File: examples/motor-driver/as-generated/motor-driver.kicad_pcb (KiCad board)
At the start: 2 copper layers, 88 x 50 mm, 12 parts, among them J1 VM 2.7-10.8V, J2 MOTOR A, J3 MOTOR B, J4 LOGIC, U1 DRV8833PW

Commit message: Arc out of a reversal at the line-out, and put the pour wedges back
Two corrections from review. The reversal now turns through every
intermediate 45 right where the line leaves the part - nine o'clock,
half-past ten, twelve, half-past one, three - by retracting along the
incoming leg and solving the arc onto the outgoing straight; the fold's
corners disappear instead of being spread, and the old three-millimetre
ride to the fan column goes with them. And the round-thirteen tongue
pruning is reverted: it was built on a misreading of the circles - the
pour filling a bent corner was never the complaint - so the fill goes
back to what the sweep makes of the copper.

Co-Authored-By: Claude Fable 5 <noreply@anthropic.com>
Claude-Session: https://claude.ai/code/session_01DUj7Ltu92tWg159mCSacwY
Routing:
- net /nFAULT: track 68.6 -> 65.3 mm
- net /nSLEEP: track 62.9 -> 59.6 mm
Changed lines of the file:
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@@
 	(segment (start 141.1375 83.725) (end 137.5 83.725) (width 0.25) (layer "F.Cu") (net 15))
 	(segment (start 137.5 83.725) (end 134.875 81.1) (width 0.25) (layer "F.Cu") (net 15))
-	(segment (start 134.875 81.1) (end 132.6 81.1) (width 0.25) (layer "F.Cu") (net 15))
-	(segment (start 132.6 81.1) (end 132.0 80.5) (width 0.25) (layer "F.Cu") (net 15))
-	(segment (start 132.0 80.5) (end 132.0 79.9) (width 0.25) (layer "F.Cu") (net 15))
-	(segment (start 132.0 79.9) (end 133.4 78.5) (width 0.25) (layer "F.Cu") (net 15))
-	(segment (start 133.4 78.5) (end 134.5 78.5) (width 0.25) (layer "F.Cu") (net 15))
+	(segment (start 134.875 81.1) (end 134.575 81.1) (width 0.25) (layer "F.Cu") (net 15))
+	(segment (start 134.575 81.1) (end 133.7915 80.3165) (width 0.25) (layer "F.Cu") (net 15))
+	(segment (start 133.7915 80.3165) (end 133.7915 79.2085) (width 0.25) (layer "F.Cu") (net 15))
+	(segment (start 133.7915 79.2085) (end 134.5 78.5) (width 0.25) (layer "F.Cu") (net 15))
 	(segment (start 134.5 78.5) (end 173.75 78.5) (width 0.25) (layer "F.Cu") (net 15))
 	(segment (start 173.75 78.5) (end 176.75 81.5) (width 0.25) (layer "F.Cu") (net 15))
@@
 	(segment (start 141.1375 88.275) (end 137.5 88.275) (width 0.25) (layer "F.Cu") (net 14))
 	(segment (start 137.5 88.275) (end 134.875 90.9) (width 0.25) (layer "F.Cu") (net 14))
-	(segment (start 134.875 90.9) (end 132.6 90.9) (width 0.25) (layer "F.Cu") (net 14))
-	(segment (start 132.6 90.9) (end 132.0 91.5) (width 0.25) (layer "F.Cu") (net 14))
-	(segment (start 132.0 91.5) (end 132.0 92.1) (width 0.25) (layer "F.Cu") (net 14))
-	(segment (start 132.0 92.1) (end 141.4 101.5) (width 0.25) (layer "F.Cu") (net 14))
-	(segment (start 141.4 101.5) (end 142.5 101.5) (width 0.25) (layer "F.Cu") (net 14))
+	(segment (start 134.875 90.9) (end 134.575 90.9) (width 0.25) (layer "F.Cu") (net 14))
+	(segment (start 134.575 90.9) (end 133.7915 91.6835) (width 0.25) (layer "F.Cu") (net 14))
+	(segment (start 133.7915 91.6835) (end 133.7915 92.7915) (width 0.25) (layer "F.Cu") (net 14))
+	(segment (start 133.7915 92.7915) (end 142.5 101.5) (width 0.25) (layer "F.Cu") (net 14))
 	(segment (start 142.5 101.5) (end 166.375 101.5) (width 0.25) (layer "F.Cu") (net 14))
 	(segment (start 166.375 101.5) (end 167.0 100.875) (width 0.25) (layer "F.Cu") (net 14))

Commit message: Stand the reversal up square at the line-out
The arc out of a fold gains one more correction from the reviewer: the
first 45 - half-past ten - made the turn read as an S. The intermediate
headings now start at 90 degrees, so the figure is the line-out, one
square stand-up, then half-past one and three, exactly as drawn.
Regenerate the motor board (the only one with such a fold) and rewrite
the REVIEW and guide passages that described the old shape.

Co-Authored-By: Claude Fable 5 <noreply@anthropic.com>
Claude-Session: https://claude.ai/code/session_01DUj7Ltu92tWg159mCSacwY
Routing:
- net /nFAULT: track 65.3 -> 64.7 mm
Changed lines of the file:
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@@
 	(segment (start 141.1375 83.725) (end 137.5 83.725) (width 0.25) (layer "F.Cu") (net 15))
 	(segment (start 137.5 83.725) (end 134.875 81.1) (width 0.25) (layer "F.Cu") (net 15))
-	(segment (start 134.875 81.1) (end 134.575 81.1) (width 0.25) (layer "F.Cu") (net 15))
-	(segment (start 134.575 81.1) (end 133.7915 80.3165) (width 0.25) (layer "F.Cu") (net 15))
-	(segment (start 133.7915 80.3165) (end 133.7915 79.2085) (width 0.25) (layer "F.Cu") (net 15))
-	(segment (start 133.7915 79.2085) (end 134.5 78.5) (width 0.25) (layer "F.Cu") (net 15))
+	(segment (start 134.875 81.1) (end 134.6 81.1) (width 0.25) (layer "F.Cu") (net 15))
+	(segment (start 134.6 81.1) (end 134.325 80.825) (width 0.25) (layer "F.Cu") (net 15))
+	(segment (start 134.325 80.825) (end 134.325 78.675) (width 0.25) (layer "F.Cu") (net 15))
+	(segment (start 134.325 78.675) (end 134.5 78.5) (width 0.25) (layer "F.Cu") (net 15))
 	(segment (start 134.5 78.5) (end 173.75 78.5) (width 0.25) (layer "F.Cu") (net 15))
 	(segment (start 173.75 78.5) (end 176.75 81.5) (width 0.25) (layer "F.Cu") (net 15))
@@
 	(segment (start 137.5 88.275) (end 134.875 90.9) (width 0.25) (layer "F.Cu") (net 14))
 	(segment (start 134.875 90.9) (end 134.575 90.9) (width 0.25) (layer "F.Cu") (net 14))
-	(segment (start 134.575 90.9) (end 133.7915 91.6835) (width 0.25) (layer "F.Cu") (net 14))
-	(segment (start 133.7915 91.6835) (end 133.7915 92.7915) (width 0.25) (layer "F.Cu") (net 14))
-	(segment (start 133.7915 92.7915) (end 142.5 101.5) (width 0.25) (layer "F.Cu") (net 14))
+	(segment (start 134.575 90.9) (end 134.575 93.575) (width 0.25) (layer "F.Cu") (net 14))
+	(segment (start 134.575 93.575) (end 142.5 101.5) (width 0.25) (layer "F.Cu") (net 14))
 	(segment (start 142.5 101.5) (end 166.375 101.5) (width 0.25) (layer "F.Cu") (net 14))
 	(segment (start 166.375 101.5) (end 167.0 100.875) (width 0.25) (layer "F.Cu") (net 14))

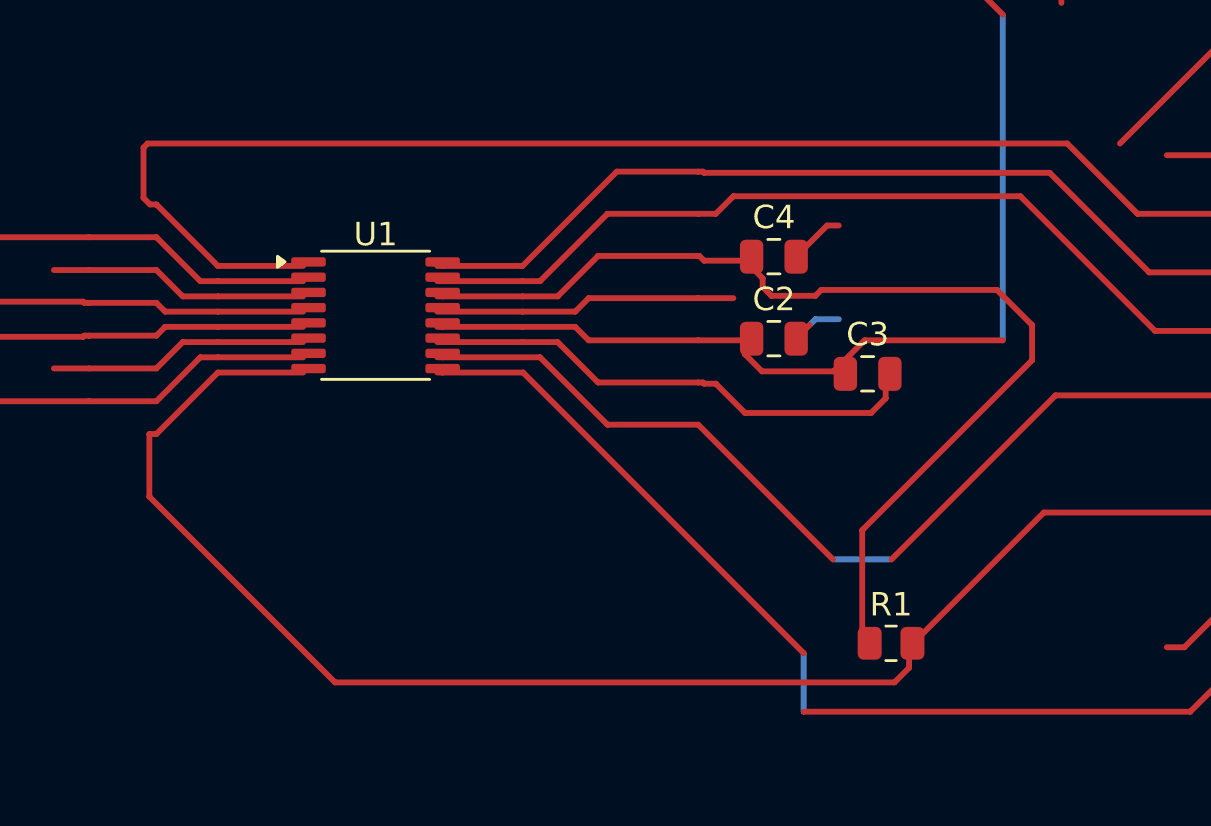
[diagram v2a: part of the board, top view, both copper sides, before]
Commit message: Start the turn at the head of the leg, with no stub at all
The reviewer's last correction on the reversal: the bend back to nine
o'clock - the lead stub the arc kept out the old heading - is not part
of the ideal figure. The turn now starts right where the incoming
straight begins, where the escape's own 45 already points the line, so
the trace draws one continuous curve from pad to bus. Two changes make
that fit: lead 0 is tried before any stub, and when the exit leg is too
short to land on without overshooting, the turn carries through the
exit's own 45 and lands on the straight beyond it.

The motor board's two reversals regenerate as equal-legged turns with
no stub; the FPGA board re-routes (the cache was lost to a container
reclaim) and reproduces its documented debt to the digit for a fourth
independent draw. The as-generated gate counts in the examples README
had drifted behind the rule set and are refreshed while the numbers
were being re-measured.

Co-Authored-By: Claude Fable 5 <noreply@anthropic.com>
Claude-Session: https://claude.ai/code/session_01DUj7Ltu92tWg159mCSacwY
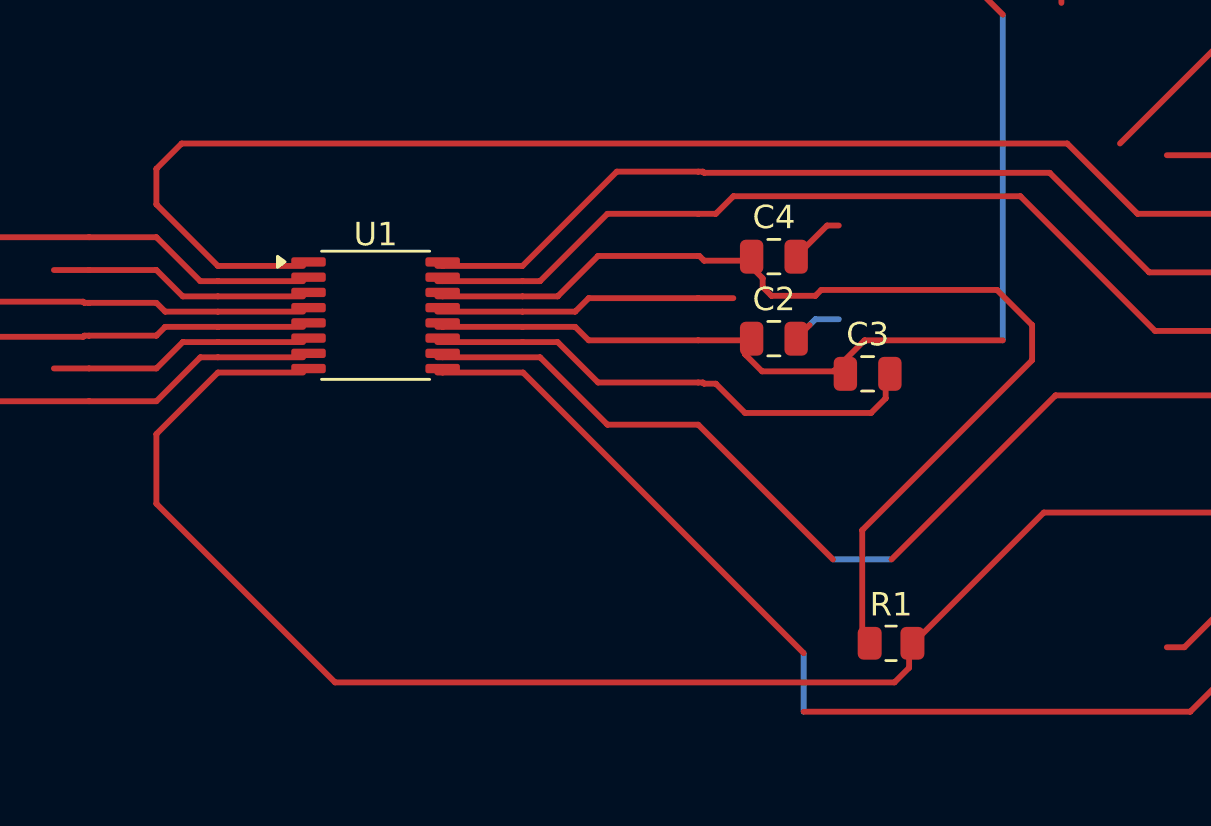
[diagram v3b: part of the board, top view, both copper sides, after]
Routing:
- net /nSLEEP: track 59.2 -> 57.7 mm
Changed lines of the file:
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@@
 	(segment (start 141.1375 83.725) (end 137.5 83.725) (width 0.25) (layer "F.Cu") (net 15))
 	(segment (start 137.5 83.725) (end 134.875 81.1) (width 0.25) (layer "F.Cu") (net 15))
-	(segment (start 134.875 81.1) (end 134.6 81.1) (width 0.25) (layer "F.Cu") (net 15))
-	(segment (start 134.6 81.1) (end 134.325 80.825) (width 0.25) (layer "F.Cu") (net 15))
-	(segment (start 134.325 80.825) (end 134.325 78.675) (width 0.25) (layer "F.Cu") (net 15))
-	(segment (start 134.325 78.675) (end 134.5 78.5) (width 0.25) (layer "F.Cu") (net 15))
-	(segment (start 134.5 78.5) (end 173.75 78.5) (width 0.25) (layer "F.Cu") (net 15))
+	(segment (start 134.875 81.1) (end 134.875 79.577) (width 0.25) (layer "F.Cu") (net 15))
+	(segment (start 134.875 79.577) (end 135.952 78.5) (width 0.25) (layer "F.Cu") (net 15))
+	(segment (start 135.952 78.5) (end 173.75 78.5) (width 0.25) (layer "F.Cu") (net 15))
 	(segment (start 173.75 78.5) (end 176.75 81.5) (width 0.25) (layer "F.Cu") (net 15))
 	(segment (start 176.75 81.5) (end 181.75 81.5) (width 0.25) (layer "F.Cu") (net 15))
@@
 	(segment (start 141.1375 88.275) (end 137.5 88.275) (width 0.25) (layer "F.Cu") (net 14))
 	(segment (start 137.5 88.275) (end 134.875 90.9) (width 0.25) (layer "F.Cu") (net 14))
-	(segment (start 134.875 90.9) (end 134.575 90.9) (width 0.25) (layer "F.Cu") (net 14))
-	(segment (start 134.575 90.9) (end 134.575 93.575) (width 0.25) (layer "F.Cu") (net 14))
-	(segment (start 134.575 93.575) (end 142.5 101.5) (width 0.25) (layer "F.Cu") (net 14))
+	(segment (start 134.875 90.9) (end 134.875 93.875) (width 0.25) (layer "F.Cu") (net 14))
+	(segment (start 134.875 93.875) (end 142.5 101.5) (width 0.25) (layer "F.Cu") (net 14))
 	(segment (start 142.5 101.5) (end 166.375 101.5) (width 0.25) (layer "F.Cu") (net 14))
 	(segment (start 166.375 101.5) (end 167.0 100.875) (width 0.25) (layer "F.Cu") (net 14))

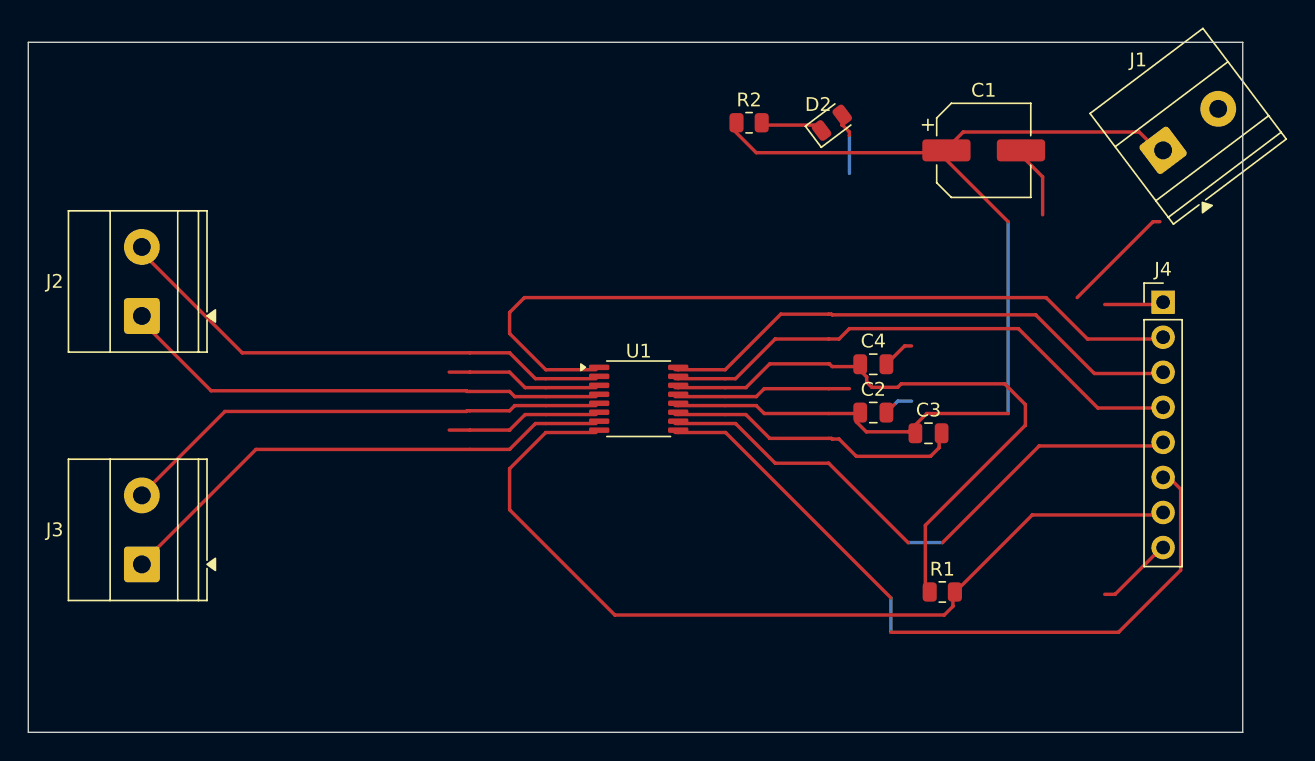
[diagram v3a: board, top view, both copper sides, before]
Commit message: Keep vias out of the lands they would drain
The reviewer's next one, and it is not one board's problem: vias were
landing inside surface-mount lands across the set. A hole in a land is a
hole solder wicks down during reflow - the joint above it starves, and
nothing on the assembled board tells that apart from a cold one.
Via-in-pad is a real technique and a filled-and-capped process, not a
drawing; a layout that has not specified the process may not draw it.

The router was the source. `_blocked` skips a route's own net, so
nothing stopped a layer change from happening on the very land the route
started at, and eighteen vias across three boards sat in one. Pads are
now marked as pads in the obstacle list and every one of them, whoever
owns it, is a cell where a via may not go - so an escape that has to
reach the plane leaves the land first and turns its via beside it. The
stitching pass kept ground vias a via-radius from ground lands where it
kept signal ones a radius plus clearance; both are the same distance
now, because the plane gains nothing from touching a land it can reach a
stub away.

`via.in_pad` measures the copper gap from every via to every land and
reports what is left. The exposed thermal pad under a package is exempt
- the via array in one is the datasheet's own answer, and nothing a
signal reaches is four square millimetres. It blocks under the
ai-generated policy: a generated board has no reason to draw this.

The test fixture had one too, a via twenty-five microns into C1's ground
land; it moves three tenths of a millimetre and the board is DRC clean
on both matrix versions as before.

Co-Authored-By: Claude Fable 5 <noreply@anthropic.com>
Claude-Session: https://claude.ai/code/session_01DUj7Ltu92tWg159mCSacwY
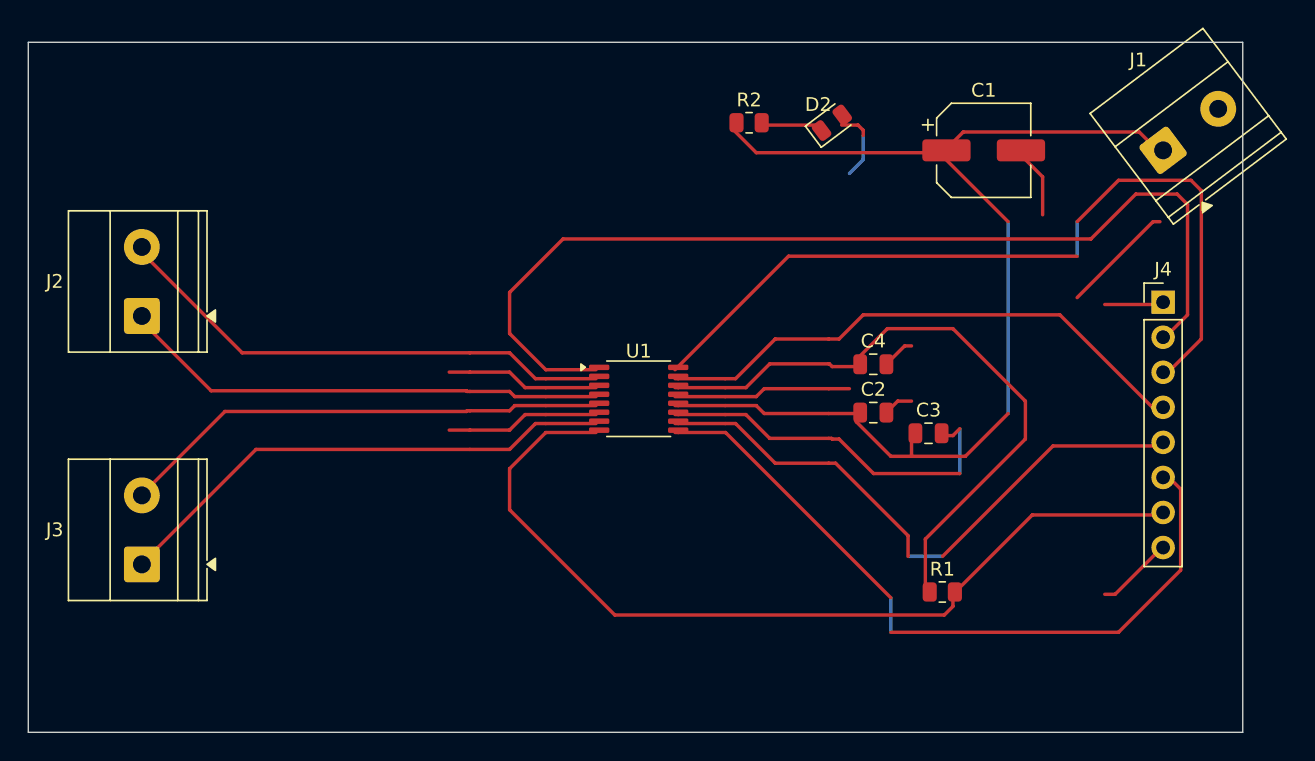
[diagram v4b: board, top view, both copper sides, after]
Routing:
- net /AIN1: track 38.6 -> 60.4 mm
- net /nSLEEP: track 57.7 -> 73.5 mm
- net /VCP: track 21.5 -> 27.4 mm
- net /VM: track 80.3 -> 83.0 mm
- net /VINT: track 44.6 -> 46.9 mm
- net /BIN2: track 41.6 -> 43.4 mm
- net GND: track 66.9 -> 68.4 mm
- net /AIN2: track 39.1 -> 39.9 mm
